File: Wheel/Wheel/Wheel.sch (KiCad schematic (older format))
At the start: 129 parts, among them J1 Conn_02x09_Odd_Even, J10 RJ45, J11 Screw_Terminal_01x02, J12 DS-201, J13 Conn_01x04, J14 Conn_02x13_Top_Bottom, J15 DB25_Female, J16 Conn_01x06, J17 Conn_01x07, J18 Conn_01x06, J19 RJ45, J2 RJ45, J20 DB9_Male, J21 DB9_Female, J22 Conn_02x15_Odd_Even, J3 RJ45, J4 RJ45, J5 USB_B, J6 Conn_02x10_Odd_Even, J7 Conn_02x09_Odd_Even, J8 RJ45, J9 RJ45, U1 MCP23S17_SP, U10 PC817, U11 IP4220CZ6, U12 PC817, U13 IP4220CZ6, U2 STM32F407VETx, U3 MCP23S17_SP, U4 USBLC6-2SC6, U5 AMS1117, U6 4N35, U7 PC817, U8 PC817, U9 PC817, Y1 32,768 кГц, Y2 8MHz

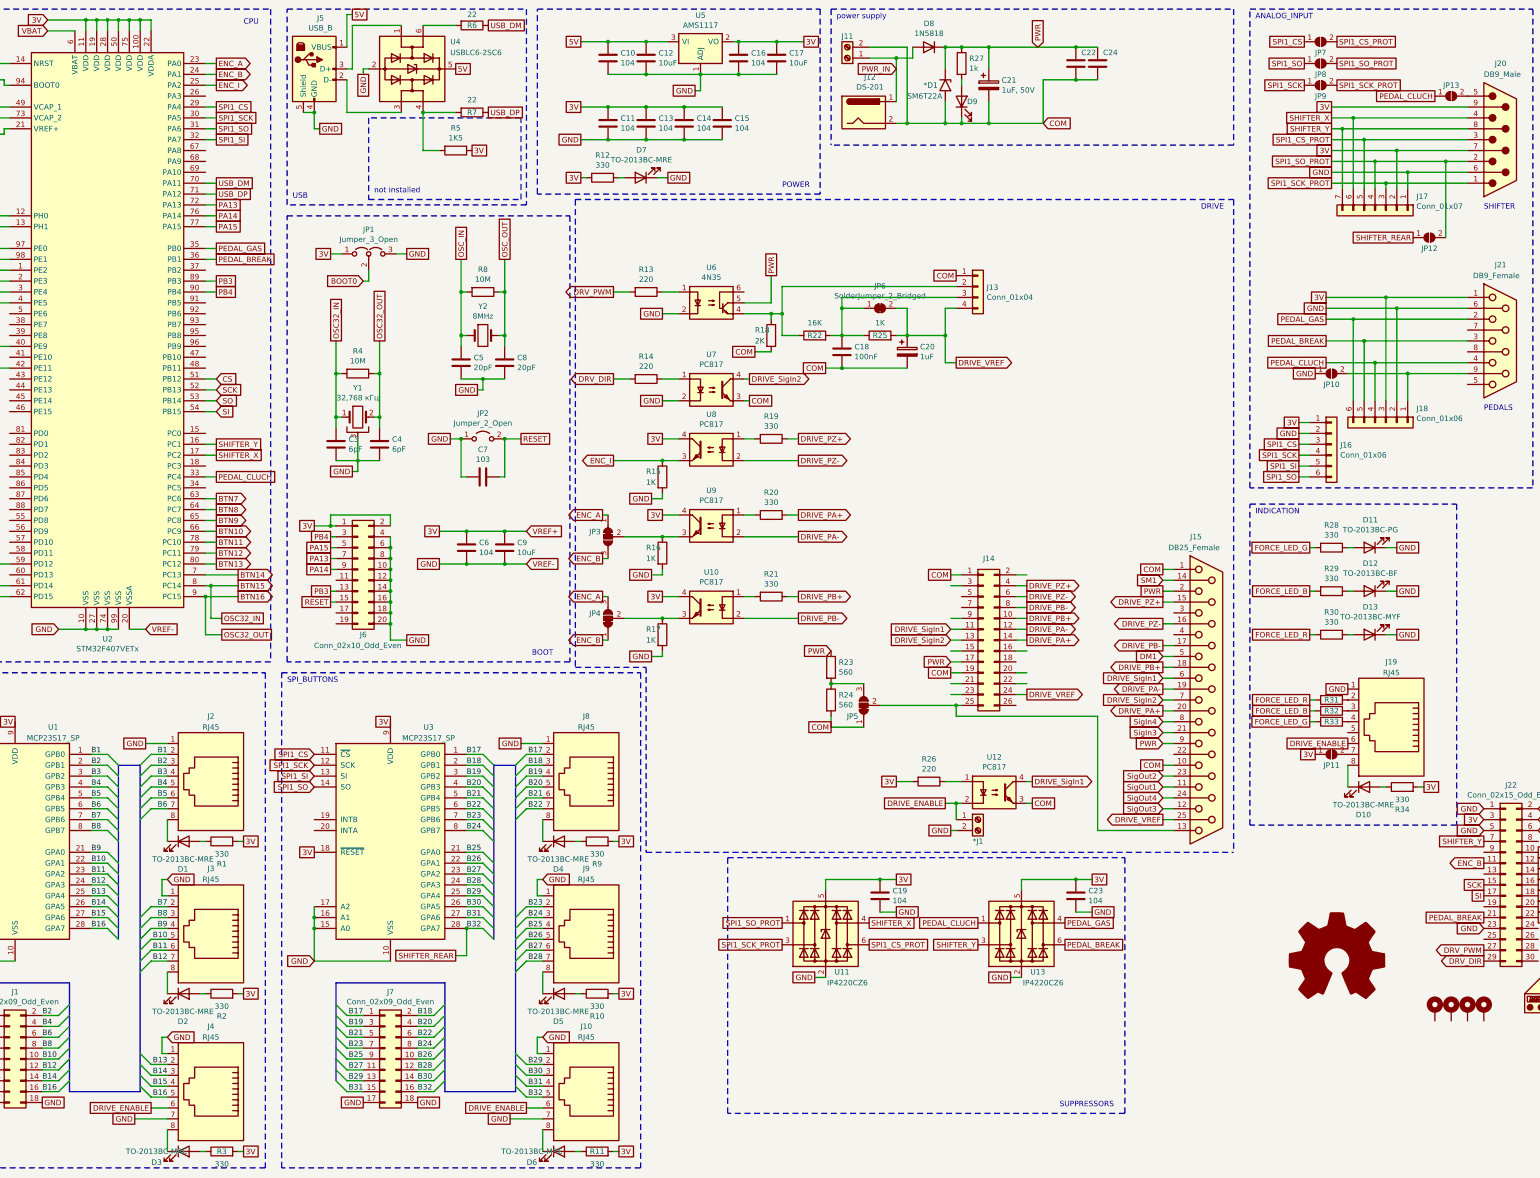
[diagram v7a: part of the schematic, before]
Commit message: I've modified Wheel's scheme and PCB
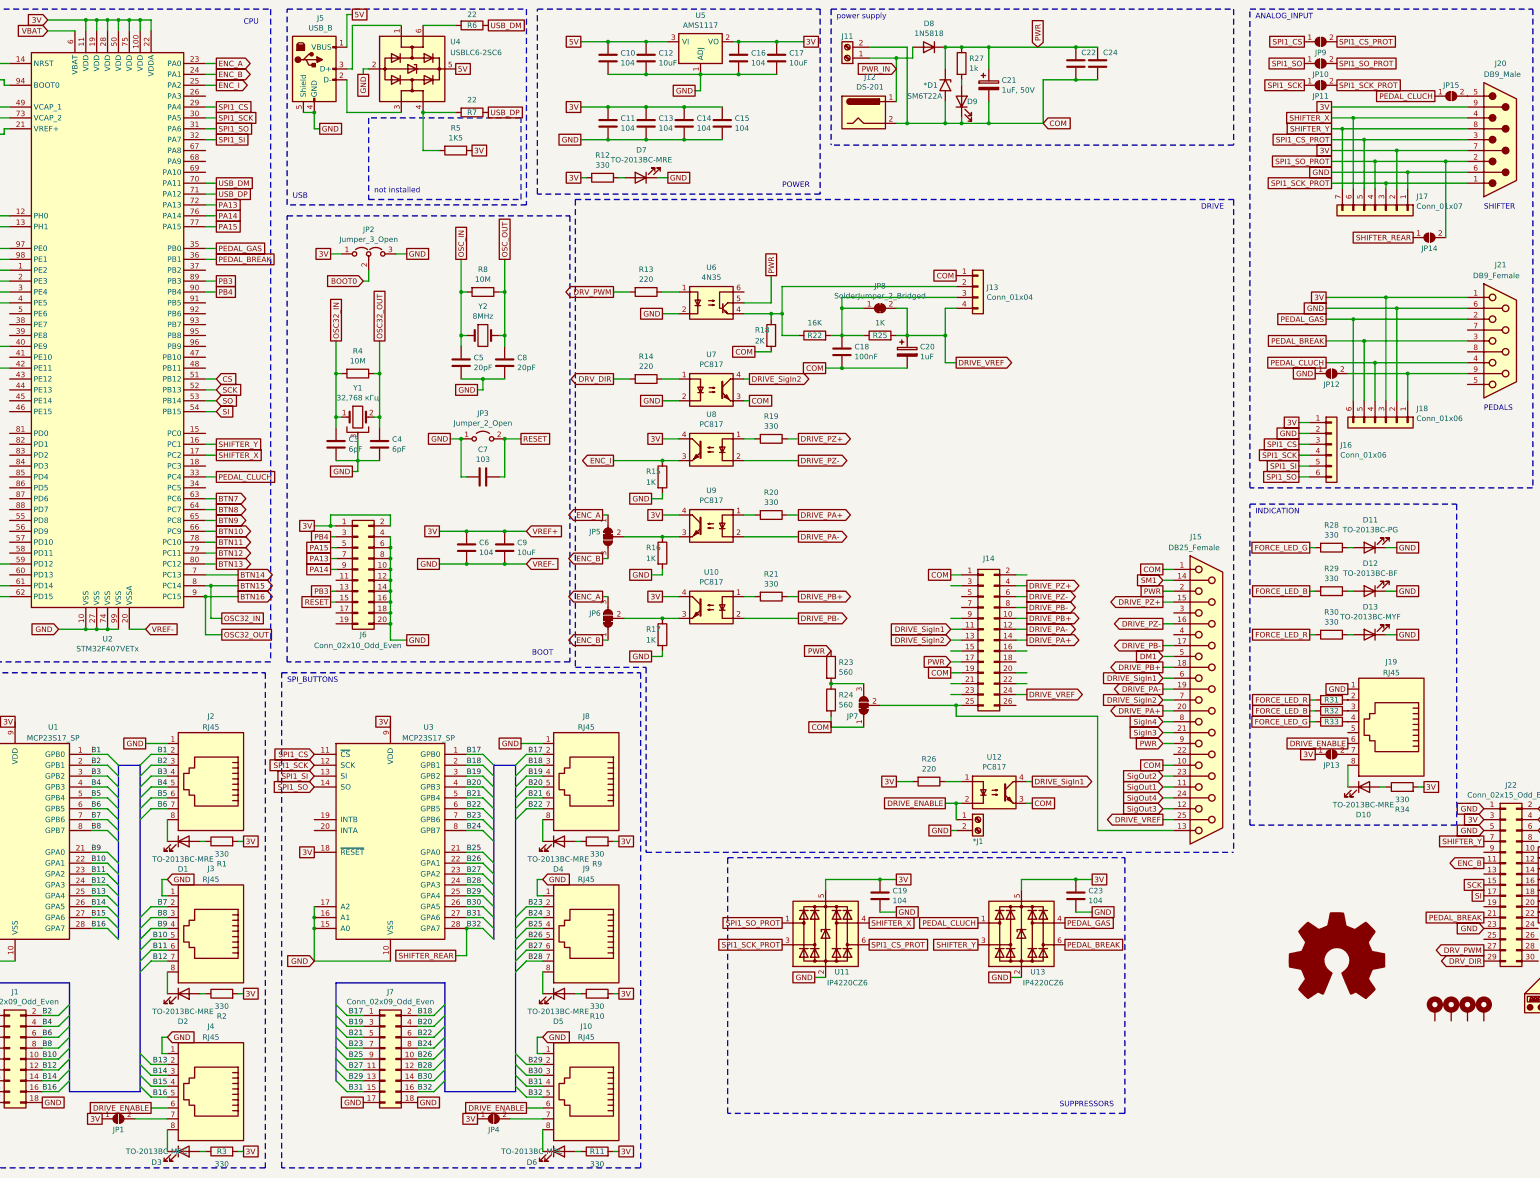
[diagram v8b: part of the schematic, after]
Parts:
- added JP1, JP4: SolderJumper_2_Open, Jumper:SolderJumper-2_P1.3mm_Open_RoundedPad1.0x1.5mm, symbol Jumper:SolderJumper_2_Open
- renumbered JP8 to JP10, JP9 to JP11, JP10 to JP12, JP11 to JP13, JP12 to JP14, JP13 to JP15, JP1 to JP2, JP2 to JP3, JP3 to JP5, JP4 to JP6, JP5 to JP7, JP6 to JP8, JP7 to JP9
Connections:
- net 3V: now also JP1.1 (A), JP4.1 (A)
- net GND: no longer J10.7, J4.7
- new net: J10.7, JP4.2 (B)
- new net: J4.7, JP1.2 (B)
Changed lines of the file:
@@
 not installed
 $Comp
-L Jumper:Jumper_3_Open JP1
+L Jumper:Jumper_3_Open JP2
 U 1 1 5FF8AC7A
 P 4750 2800
-F 0 "JP1" H 4750 3024 50  0000 C CNN
+F 0 "JP2" H 4750 3024 50  0000 C CNN
 F 1 "Jumper_3_Open" H 4750 2933 50  0000 C CNN
 F 2 "Connector_PinSocket_2.54mm:PinSocket_1x03_P2.54mm_Vertical" H 4750 2800 50  0001 C CNN
@@
 	3250 2550 3350 2550
 $Comp
-L Jumper:Jumper_2_Open JP2
+L Jumper:Jumper_2_Open JP3
 U 1 1 60037886
 P 5800 4500
-F 0 "JP2" H 5800 4735 50  0000 C CNN
+F 0 "JP3" H 5800 4735 50  0000 C CNN
 F 1 "Jumper_2_Open" H 5800 4644 50  0000 C CNN
 F 2 "Connector_PinSocket_2.54mm:PinSocket_1x02_P2.54mm_Vertical" H 5800 4500 50  0001 C CNN
@@
 	7450 5750 7450 5700
 $Comp
-L Jumper:SolderJumper_3_Bridged12 JP3
+L Jumper:SolderJumper_3_Bridged12 JP5
 U 1 1 602F5B06
 P 6950 5400
-F 0 "JP3" V 6904 5468 50  0000 L CNN
+F 0 "JP5" V 6904 5468 50  0000 L CNN
 F 1 "SolderJumper_3_Bridged12" V 6995 5468 50  0001 L CNN
 F 2 "Jumper:SolderJumper-3_P1.3mm_Bridged12_RoundedPad1.0x1.5mm" H 6950 5400 50  0001 C CNN
@@
 	7450 6500 7450 6450
 $Comp
-L Jumper:SolderJumper_3_Bridged12 JP4
+L Jumper:SolderJumper_3_Bridged12 JP6
 U 1 1 6031E70A
 P 6950 6150
-F 0 "JP4" V 6996 6218 50  0000 L CNN
+F 0 "JP6" V 6996 6218 50  0000 L CNN
 F 1 "SolderJumper_3_Bridged12" V 6905 6218 50  0001 L CNN
 F 2 "Jumper:SolderJumper-3_P1.3mm_Bridged12_RoundedPad1.0x1.5mm" H 6950 6150 50  0001 C CNN
@@
 Wire Wire Line
 	2600 10750 2900 10750
-Text GLabel 2600 10750 0    50   UnSpc ~ 0
-GND
 Text Label 2200 7400 0    50   ~ 0
 B1
@@
 	13400 7100 13450 7100
 $Comp
-L Jumper:SolderJumper_2_Open JP10
+L Jumper:SolderJumper_2_Open JP12
 U 1 1 64145DC0
 P 13600 3900
-F 0 "JP10" H 13600 3800 50  0000 C CNN
+F 0 "JP12" H 13600 3800 50  0000 C CNN
 F 1 "SolderJumper_2_Open" H 13600 4014 50  0001 C CNN
 F 2 "Jumper:SolderJumper-2_P1.3mm_Open_RoundedPad1.0x1.5mm" H 13600 3900 50  0001 C CNN
@@
 	14200 3300 14850 3300
 $Comp
-L Jumper:SolderJumper_2_Bridged JP6
+L Jumper:SolderJumper_2_Bridged JP8
 U 1 1 60359245
 P 9450 3300
-F 0 "JP6" H 9450 3505 50  0000 C CNN
+F 0 "JP8" H 9450 3505 50  0000 C CNN
 F 1 "SolderJumper_2_Bridged" H 9450 3414 50  0000 C CNN
 F 2 "Jumper:SolderJumper-2_P1.3mm_Bridged_RoundedPad1.0x1.5mm" H 9450 3300 50  0001 C CNN
@@
 Wire Wire Line
 	6050 10750 6350 10750
-Text GLabel 6050 10750 0    50   UnSpc ~ 0
-GND
 Text Label 5650 7400 0    50   ~ 0
 B17
@@
 	13900 1750 14850 1750
 $Comp
-L Jumper:SolderJumper_2_Open JP8
+L Jumper:SolderJumper_2_Open JP10
 U 1 1 5FFF5B9C
 P 13500 1050
-F 0 "JP8" H 13500 950 50  0000 C CNN
+F 0 "JP10" H 13500 950 50  0000 C CNN
 F 1 "SolderJumper_2_Open" H 13500 1164 50  0001 C CNN
 F 2 "Jumper:SolderJumper-2_P1.3mm_Open_RoundedPad1.0x1.5mm" H 13500 1050 50  0001 C CNN
@@
 $EndComp
 $Comp
-L Jumper:SolderJumper_2_Open JP9
+L Jumper:SolderJumper_2_Open JP11
 U 1 1 5FFF60EF
 P 13500 1250
-F 0 "JP9" H 13500 1150 50  0000 C CNN
+F 0 "JP11" H 13500 1150 50  0000 C CNN
 F 1 "SolderJumper_2_Open" H 13500 1364 50  0001 C CNN
 F 2 "Jumper:SolderJumper-2_P1.3mm_Open_RoundedPad1.0x1.5mm" H 13500 1250 50  0001 C CNN
@@
 $EndComp
 $Comp
-L Jumper:SolderJumper_3_Bridged12 JP5
+L Jumper:SolderJumper_3_Bridged12 JP7
 U 1 1 6013722B
 P 9300 6950
-F 0 "JP5" V 9200 7000 50  0000 L CNN
+F 0 "JP7" V 9200 7000 50  0000 L CNN
 F 1 "SolderJumper_3_Bridged12" V 9255 7018 50  0001 L CNN
 F 2 "Jumper:SolderJumper-3_P1.3mm_Bridged12_RoundedPad1.0x1.5mm" H 9300 6950 50  0001 C CNN
@@
 SPI1_CS
 $Comp
-L Jumper:SolderJumper_2_Open JP7
+L Jumper:SolderJumper_2_Open JP9
 U 1 1 6057F306
 P 13500 850
-F 0 "JP7" H 13500 750 50  0000 C CNN
+F 0 "JP9" H 13500 750 50  0000 C CNN
 F 1 "SolderJumper_2_Open" H 13500 964 50  0001 C CNN
 F 2 "Jumper:SolderJumper-2_P1.3mm_Open_RoundedPad1.0x1.5mm" H 13500 850 50  0001 C CNN
@@
 $EndComp
 $Comp
-L Jumper:SolderJumper_2_Open JP11
+L Jumper:SolderJumper_2_Open JP13
 U 1 1 600C876D
 P 13600 7400
-F 0 "JP11" H 13600 7300 50  0000 C CNN
+F 0 "JP13" H 13600 7300 50  0000 C CNN
 F 1 "SolderJumper_2_Open" H 13600 7514 50  0001 C CNN
 F 2 "Jumper:SolderJumper-2_P1.3mm_Open_RoundedPad1.0x1.5mm" H 13600 7400 50  0001 C CNN
@@
 3V
 $Comp
-L Jumper:SolderJumper_2_Open JP13
+L Jumper:SolderJumper_2_Open JP15
 U 1 1 600CA850
 P 14700 1350
-F 0 "JP13" H 14700 1450 50  0000 C CNN
+F 0 "JP15" H 14700 1450 50  0000 C CNN
 F 1 "SolderJumper_2_Open" H 14700 1464 50  0001 C CNN
 F 2 "Jumper:SolderJumper-2_P1.3mm_Open_RoundedPad1.0x1.5mm" H 14700 1350 50  0001 C CNN
@@
 PEDAL_CLUCH
 $Comp
-L Jumper:SolderJumper_2_Open JP12
+L Jumper:SolderJumper_2_Open JP14
 U 1 1 6019891C
 P 14500 2650
-F 0 "JP12" H 14500 2550 50  0000 C CNN
+F 0 "JP14" H 14500 2550 50  0000 C CNN
 F 1 "SolderJumper_2_Open" H 14500 2764 50  0001 C CNN
 F 2 "Jumper:SolderJumper-2_P1.3mm_Open_RoundedPad1.0x1.5mm" H 14500 2650 50  0001 C CNN
@@
 Wire Wire Line
 	5650 9250 5650 9000
+Connection ~ 5650 9000
+$Comp
+L Jumper:SolderJumper_2_Open JP4
+U 1 1 600CDBB9
+P 5900 10750
+F 0 "JP4" H 5900 10650 50  0000 C CNN
+F 1 "SolderJumper_2_Open" H 5900 10864 50  0001 C CNN
+F 2 "Jumper:SolderJumper-2_P1.3mm_Open_RoundedPad1.0x1.5mm" H 5900 10750 50  0001 C CNN
+F 3 "~" H 5900 10750 50  0001 C CNN
+	1    5900 10750
+	1    0    0    -1
+$EndComp
+Text GLabel 5750 10750 0    50   UnSpc ~ 0
+3V
+$Comp
+L Jumper:SolderJumper_2_Open JP1
+U 1 1 600D0079
+P 2450 10750
+F 0 "JP1" H 2450 10650 50  0000 C CNN
+F 1 "SolderJumper_2_Open" H 2450 10864 50  0001 C CNN
+F 2 "Jumper:SolderJumper-2_P1.3mm_Open_RoundedPad1.0x1.5mm" H 2450 10750 50  0001 C CNN
+F 3 "~" H 2450 10750 50  0001 C CNN
+	1    2450 10750
+	1    0    0    -1
+$EndComp
+Text GLabel 2300 10750 0    50   UnSpc ~ 0
+3V
 Wire Bus Line
 	4450 9500 4450 10400
@@
 Wire Bus Line
 	2650 7500 2650 10500
-Connection ~ 5650 9000
 $EndSCHEMATC
